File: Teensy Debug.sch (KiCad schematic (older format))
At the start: 3 parts, among them J1 Conn_02x07_Odd_Even, U1 MKL02Z32VFG4, U2 MKL02Z32VFG4

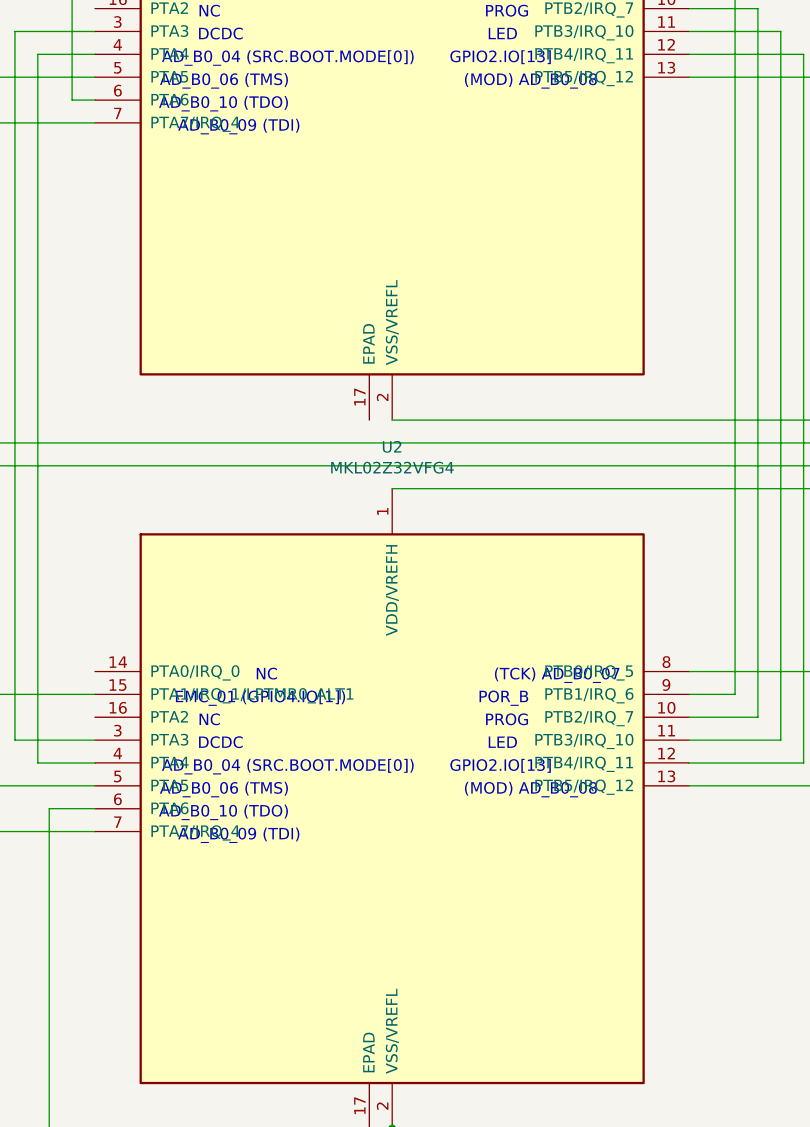
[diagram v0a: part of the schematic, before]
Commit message: Schematic Labels
Add labels to Teensy & MKL02
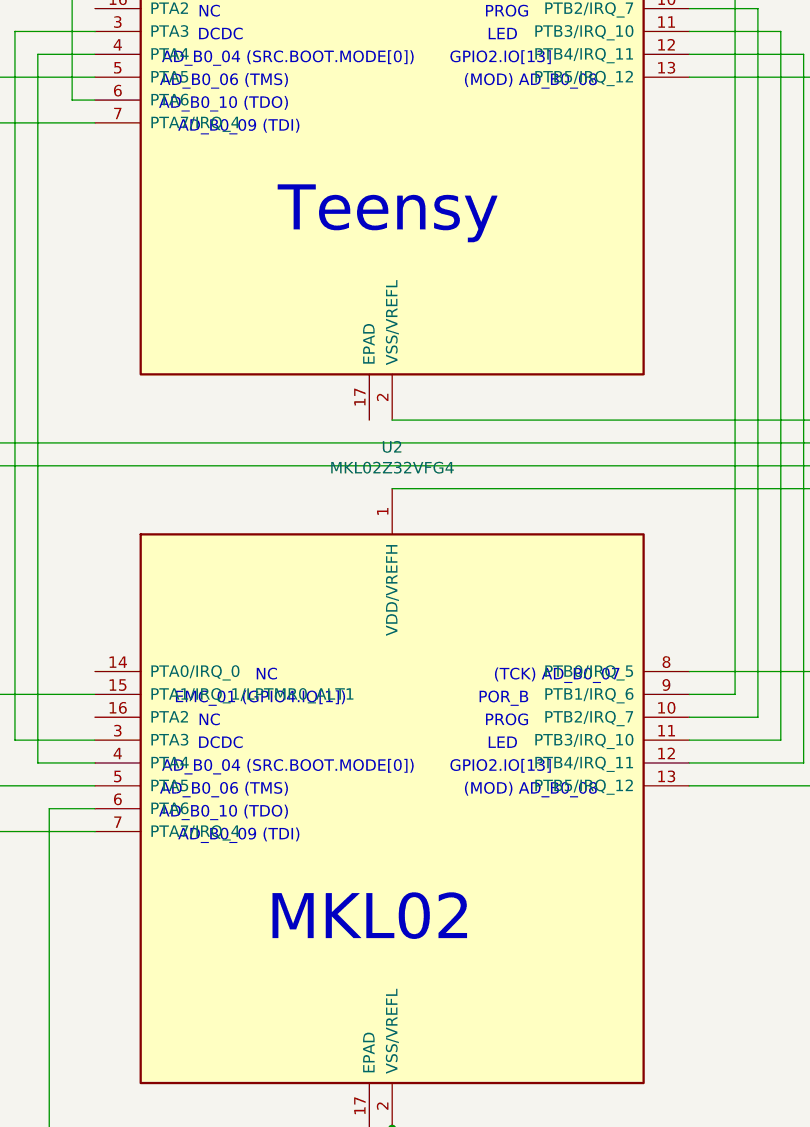
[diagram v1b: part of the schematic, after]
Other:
- note added: "MKL02"
- note added: "Teensy"
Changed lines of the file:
@@
 Text Notes 3650 5750 2    50   ~ 0
 (MOD) AD_B0_08
+Text Notes 2250 3300 0    197  ~ 0
+Teensy
+Text Notes 2200 6400 0    197  ~ 0
+MKL02
 $EndSCHEMATC
